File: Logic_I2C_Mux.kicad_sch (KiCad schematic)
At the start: 14 parts, among them U801 TCA9546APWR

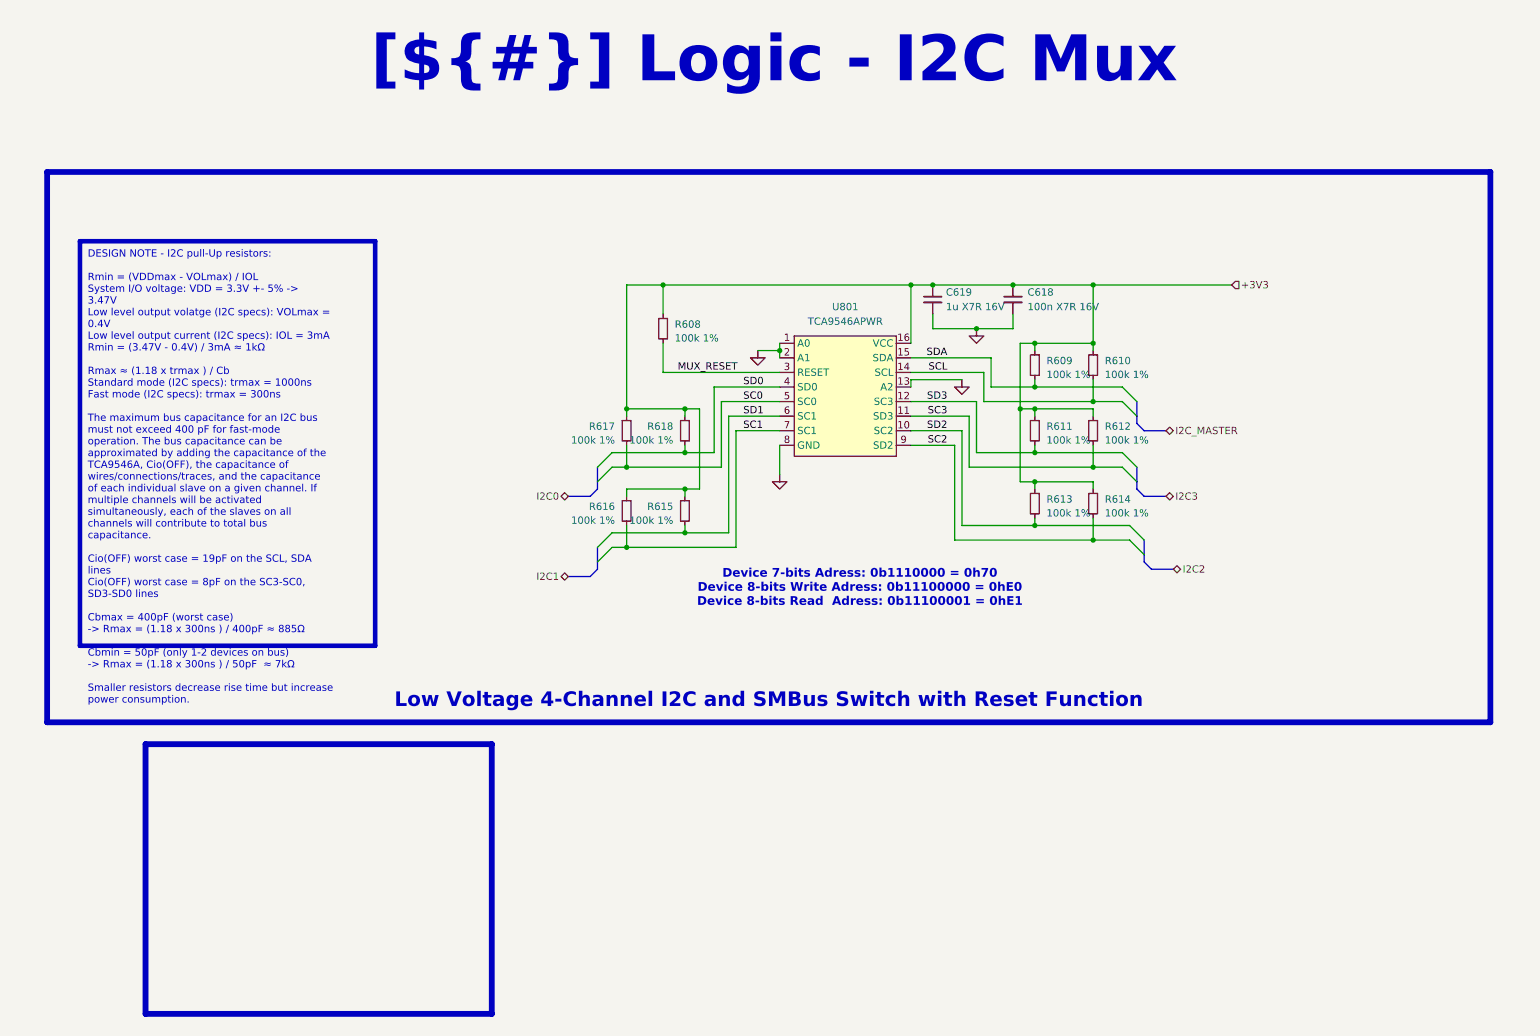
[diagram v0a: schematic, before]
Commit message: Added footprints, images, almost finished all èages except for the MCU
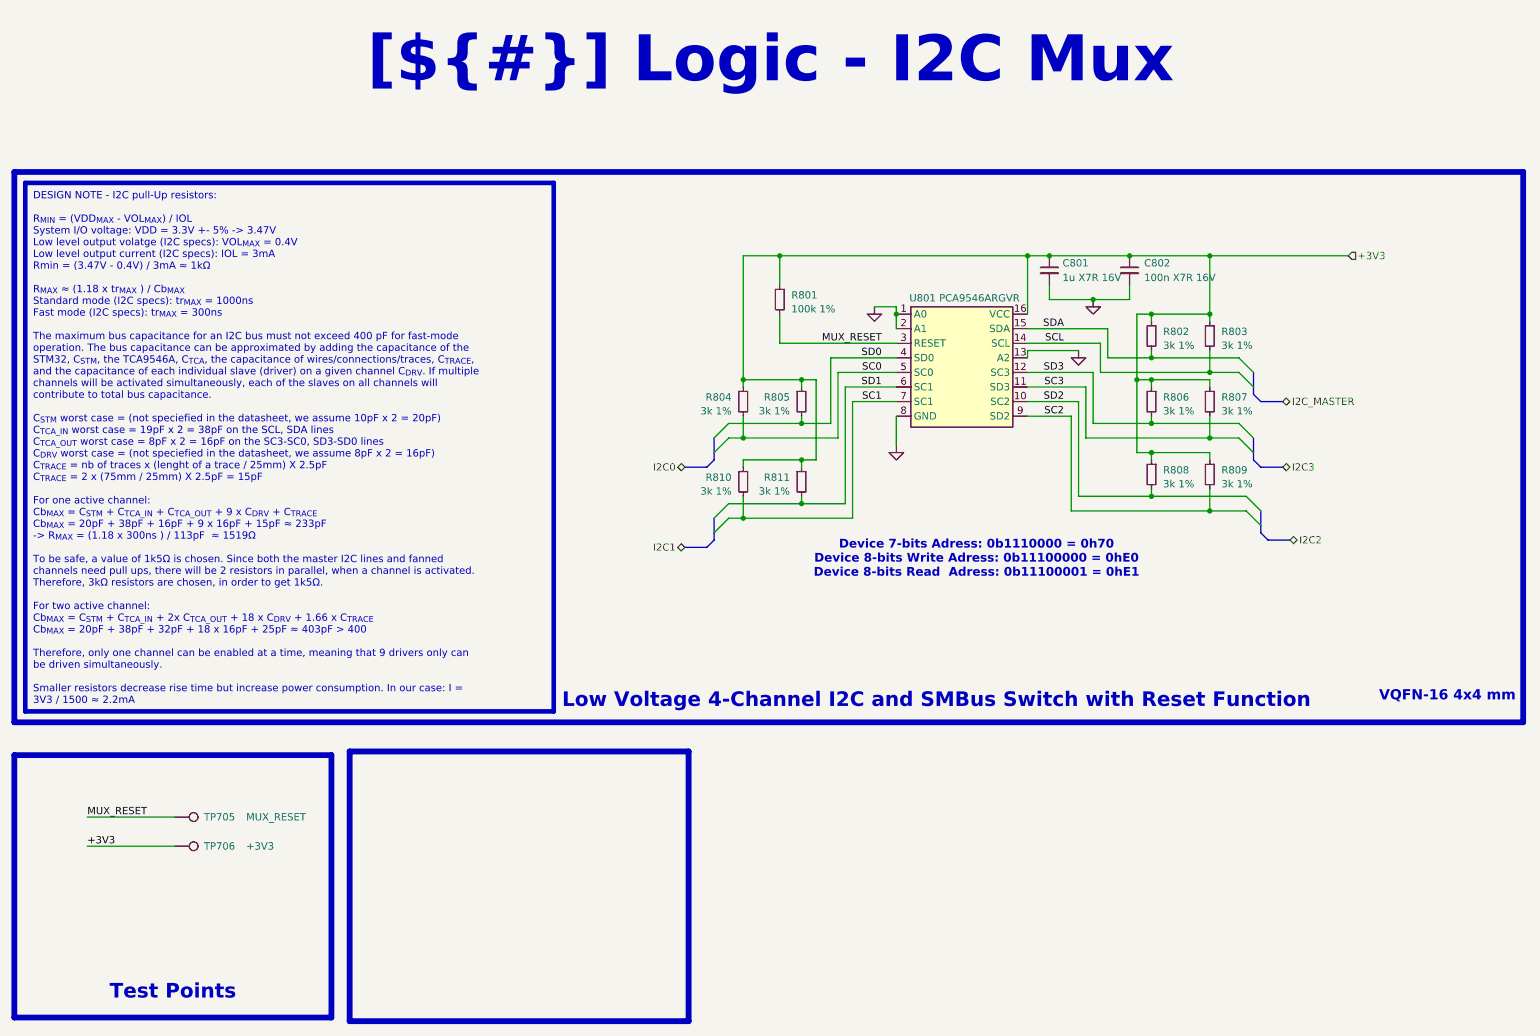
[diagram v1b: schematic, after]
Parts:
- removed R609, R610, R611, R612, R613, R614, R615, R616, R618: 100k 1%, Resistor_SMD:R_0402_1005Metric, symbol Device:R_Small
- added R802, R803, R805, R806, R807, R808, R809, R810, R811: 3k 1%, Resistor_SMD:R_0402_1005Metric, symbol Device:R_Small
- added TP705: MUX_RESET, 0_Zenith:TestPoint_Pad_D0.5mm_Front, symbol Connector:TestPoint
- added TP706: +3V3, 0_Zenith:TestPoint_Pad_D0.5mm_Front, symbol Connector:TestPoint
- R804: renamed from R617; value 100k 1% -> 3k 1%; Manufacturer Panasonic -> KOA Speer; Manufacturer Part Number ERJ-2RKF1003X -> RK73H1ETTP3001F; Supplier Part Number 667-ERJ-2RKF1003X -> 660-RK73H1ETTP3001F
- U801: value TCA9546APWR -> PCA9546ARGVR; footprint Package_SO:TSSOP-16_4.4x5mm_P0.65mm -> 0_Plume:Texas_RSA_VQFN-16-1EP_4x4mm_P0.65mm_EP2.16x2.16mm; Manufacturer (none) -> Texas Instruments; Manufacturer Part Number (none) -> PCA9546ARGVR; Supplier (none) -> Mouser Electronics; Supplier Part Number (none) -> 595-PCA9546ARGVR
- renumbered C619 to C801, C618 to C802, R608 to R801
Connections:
- net +3V3: now also R802.1, R803.1, R805.1, R806.1, R807.1, R808.1, R809.1, R810.1, R811.1, TP706.1
- net MUX_RESET: now also TP705.1
- net SC1: now also R810.2
- net SC2: now also R809.2
- net SC3: now also R807.2
- net SCL: now also R803.2
- net SD0: now also R805.2
- net SD1: now also R811.2
- net SD2: now also R808.2
- net SD3: now also R806.2
- net SDA: now also R802.2
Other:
- note added: "VQFN-16 4x4 mm"
- moved on the sheet: C801, C802, R801, R804, U801

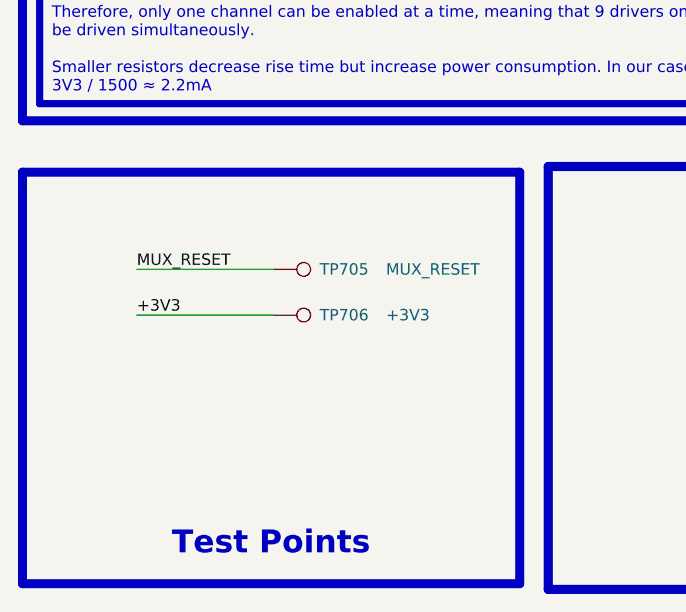
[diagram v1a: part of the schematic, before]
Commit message: Added RGB LED, added motor connectors, added test points, imported all 3D models
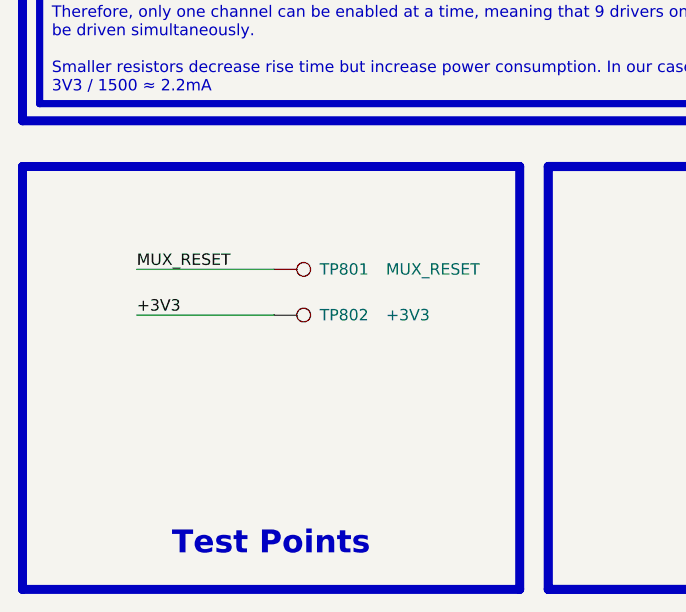
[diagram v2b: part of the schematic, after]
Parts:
- TP801: renamed from TP705; footprint 0_Zenith:TestPoint_Pad_D0.5mm_Front -> 0_Plume:TestPoint_Pad_D0.5mm_Back
- TP802: renamed from TP706; footprint 0_Zenith:TestPoint_Pad_D0.5mm_Front -> 0_Plume:TestPoint_Pad_D0.5mm_Back

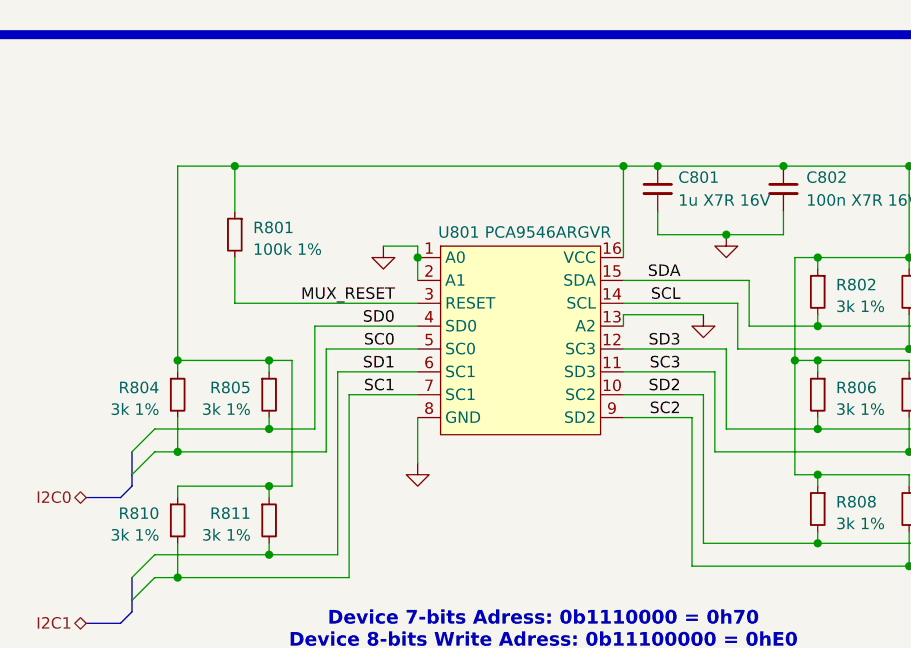
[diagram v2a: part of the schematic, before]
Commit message: Finished schematic, imported all footprints, all 3D models and created STM32 project, now need to proofread shematic before layout
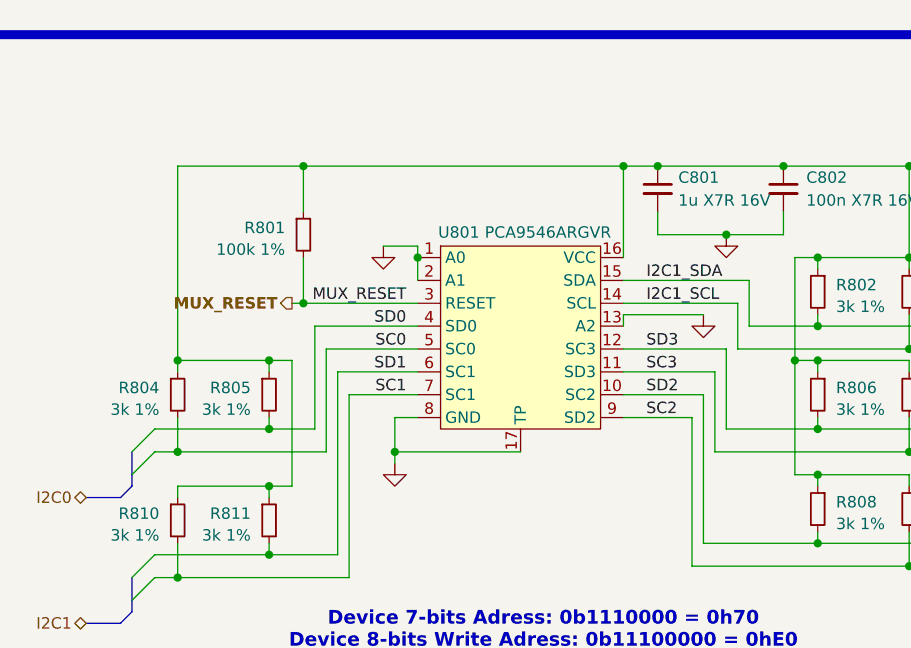
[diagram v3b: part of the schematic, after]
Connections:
- net GND: now also U801.17 (TP)
- net SCL renamed I2C1_SCL
- net SDA renamed I2C1_SDA
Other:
- moved on the sheet: R801
